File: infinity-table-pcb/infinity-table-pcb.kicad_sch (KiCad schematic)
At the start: 10 parts, among them J1 PJ-063AH, J2 Conn_01x05_Male, J3 Conn_01x10_Male

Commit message: forgot to save work
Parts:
- removed C1: 100nF, Capacitor_SMD:C_0805_2012Metric, symbol Device:C
- removed IO2, IO3, IO5, IO6: SolderJumper_3_Open, Jumper:SolderJumper-3_P1.3mm_Open_Pad1.0x1.5mm, symbol Jumper:SolderJumper_3_Open
- removed J2: Conn_01x05_Male, Connector_PinHeader_2.54mm:PinHeader_1x05_P2.54mm_Vertical, symbol Connector:Conn_01x05_Male
- removed J3: Conn_01x10_Male, Connector_PinHeader_2.54mm:PinHeader_1x10_P2.54mm_Vertical, symbol Connector:Conn_01x10_Male
- added RV?: R_Potentiometer, symbol Device:R_Potentiometer
- added U?: 74LVC8T245, symbol 74LVC8T245:74LVC8T245
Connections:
- net GND: now also RV?.1, U?.11 (GND), U?.12 (GND), U?.13 (GND)
- net at A1.19 (A0): now also RV?.2
- net +5V: now reaches A1.27 (+5V), C2.1
- net +5V: now also J1.1, RV?.3
- net D0: no longer names the net of A1.2 (D0/RX)
- net D1: no longer names the net of A1.1 (D1/TX)
- net D10: no longer names the net of A1.13 (D10)
- net D2: no longer names the net of A1.5 (D2)
- net D3: no longer names the net of A1.6 (D3)
- net D5: no longer names the net of A1.8 (D5)
- net D6: no longer names the net of A1.9 (D6)
- net D9: no longer names the net of A1.12 (D9)
- no-connect marks 15 -> 18
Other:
- moved on the sheet: C2, J1

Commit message: wip infinity-table-pcb
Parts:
- removed U?: 74LVC8T245, symbol 74LVC8T245:74LVC8T245
- added C? (x2): 1nF, Capacitor_SMD:C_0805_2012Metric, symbol Device:C
- added C? (x2): 0,1nF, Capacitor_SMD:C_0805_2012Metric, symbol Device:C
- added J?: Conn_01x04_Male, symbol Connector:Conn_01x04_Male
- added J?: Conn_01x10_Male, symbol Connector:Conn_01x10_Male
- added SW? (x2): SW_Push_Dual, symbol Switch:SW_Push_Dual
- added U?: TXS0108EPW, Package_SO:TSSOP-20_4.4x6.5mm_P0.65mm, symbol Logic_LevelTranslator:TXS0108EPW
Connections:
- net +5V: now also C?.2, J?.2 (Pin_2), U?.2 (VCCA)
- net GND: now also C?.1, C?.1, C?.2, C?.2, J?.1 (Pin_1), J?.1 (Pin_1), SW?.2, SW?.2, SW?.4, SW?.4, U?.10 (OE), U?.11 (GND); no longer A1.29 (GND)
- net at A1.10 (D7): now also U?.3 (A2)
- net at A1.11 (D8): now also U?.4 (A3)
- net at A1.12 (D9): now also U?.5 (A4)
- net at A1.13 (D10): now also U?.6 (A5)
- net at A1.14 (D11): now also U?.7 (A6)
- net at A1.15 (D12): now also U?.8 (A7)
- net at A1.16 (D13): now also U?.9 (A8)
- net at A1.6 (D3): now also J?.3 (Pin_3)
- net SW1: now reaches A1.7 (D4)
- net SW1: now also C?.2, SW?.1, SW?.3
- net SW2: now reaches A1.8 (D5)
- net SW2: now also C?.1, SW?.1, SW?.3
- net at A1.9 (D6): now also U?.1 (A1)
- new net: J?.2 (Pin_2), U?.12 (B8)
- new net: J?.3 (Pin_3), U?.13 (B7)
- new net: J?.4 (Pin_4), U?.14 (B6)
- new net: J?.5 (Pin_5), U?.15 (B5)
- new net: J?.6 (Pin_6), U?.16 (B4)
- new net: J?.7 (Pin_7), U?.17 (B3)
- new net: J?.8 (Pin_8), U?.18 (B2)
- new net: C?.1, J?.10 (Pin_10), U?.19 (VCCB)
- new net: J?.9 (Pin_9), U?.20 (B1)
- no-connect marks 18 -> 15
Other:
- note added: "LED connector"
- note added: "Level shifter"
- moved on the sheet: A1, C2, J1, RV?

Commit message: pcb first version done, but need to rework a bit
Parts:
- removed C2: 100nF, Capacitor_SMD:C_0805_2012Metric, symbol Device:C
- added R1: R, Resistor_SMD:R_0805_2012Metric, symbol Device:R
- C1, C3: renamed from C?; value 0,1nF -> 0,1uF
- J1: footprint SS_connectors:CUI_PJ-063AH-1 -> kicad-ss-libs:CUI_PJ-063AH
- J2: renamed from J?; footprint (none) -> Connector_PinHeader_2.54mm:PinHeader_1x04_P2.54mm_Vertical
- J3: renamed from J?; footprint (none) -> Connector_PinHeader_2.54mm:PinHeader_1x10_P2.54mm_Vertical
- RV1: renamed from RV?; footprint (none) -> Connector_PinHeader_2.54mm:PinHeader_1x03_P2.54mm_Vertical
- SW1, SW2: renamed from SW?; footprint (none) -> kicad-ss-libs:Push Button 12x12mm
- gave numbers to parts that had none: 3
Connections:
- net +5V: now also U1.19 (VCCB); no longer U1.2 (VCCA)
- net GND: now also A1.29 (GND), R1.2; no longer U1.10 (OE)
- net SW1: now also A1.8 (D5); no longer A1.7 (D4), SW1.3
- net SW2: now also A1.7 (D4); no longer A1.8 (D5), SW2.1
- net at A1.10 (D7): now also U1.18 (B2); no longer U1.3 (A2)
- net at A1.11 (D8): now also U1.17 (B3); no longer U1.4 (A3)
- net at A1.12 (D9): now also U1.16 (B4); no longer U1.5 (A4)
- net at A1.13 (D10): now also U1.15 (B5); no longer U1.6 (A5)
- net at A1.14 (D11): now also U1.14 (B6); no longer U1.7 (A6)
- net at A1.15 (D12): now also U1.13 (B7); no longer U1.8 (A7)
- net at A1.16 (D13): now also U1.12 (B8); no longer U1.9 (A8)
- net at A1.9 (D6): now also U1.20 (B1); no longer U1.1 (A1)
- net at J3.2 (Pin_2): now also U1.9 (A8); no longer U1.12 (B8)
- net at J3.3 (Pin_3): now also U1.8 (A7); no longer U1.13 (B7)
- net at J3.4 (Pin_4): now also U1.7 (A6); no longer U1.14 (B6)
- net at J3.5 (Pin_5): now also U1.6 (A5); no longer U1.15 (B5)
- net at J3.6 (Pin_6): now also U1.5 (A4); no longer U1.16 (B4)
- net at J3.7 (Pin_7): now also U1.4 (A3); no longer U1.17 (B3)
- net at J3.8 (Pin_8): now also U1.3 (A2); no longer U1.18 (B2)
- net at C3.1, J3.10 (Pin_10): now also U1.10 (OE), U1.2 (VCCA), R1.1; no longer U1.19 (VCCB)
- net at J3.9 (Pin_9): now also U1.1 (A1); no longer U1.20 (B1)
- no-connect marks 15 -> 18
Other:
- moved on the sheet: C1, J3

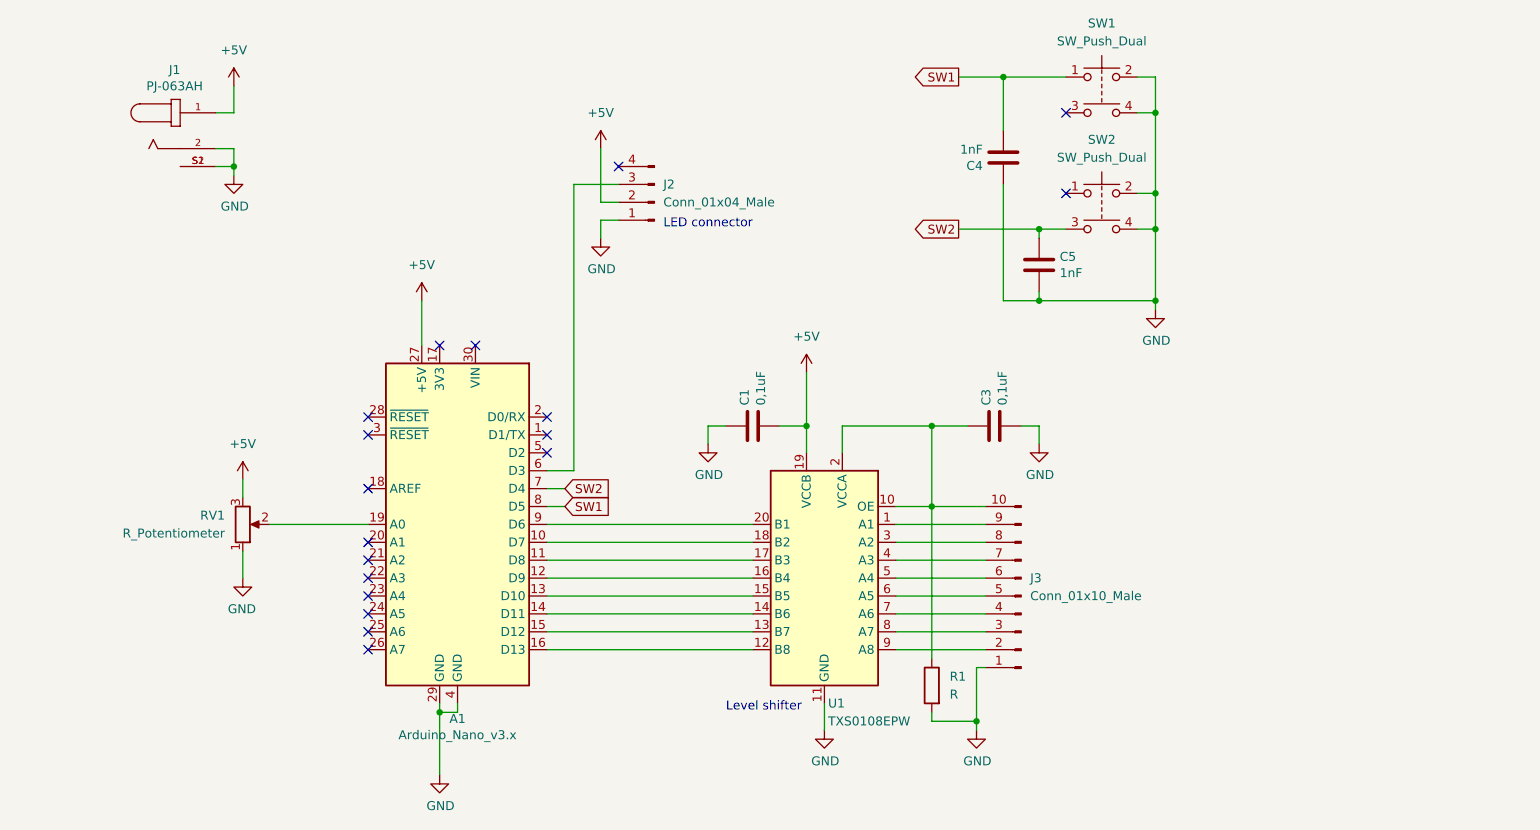
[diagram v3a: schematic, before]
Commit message: pcb ver 2 done. Maybe potentiometer footprint needs to be checked
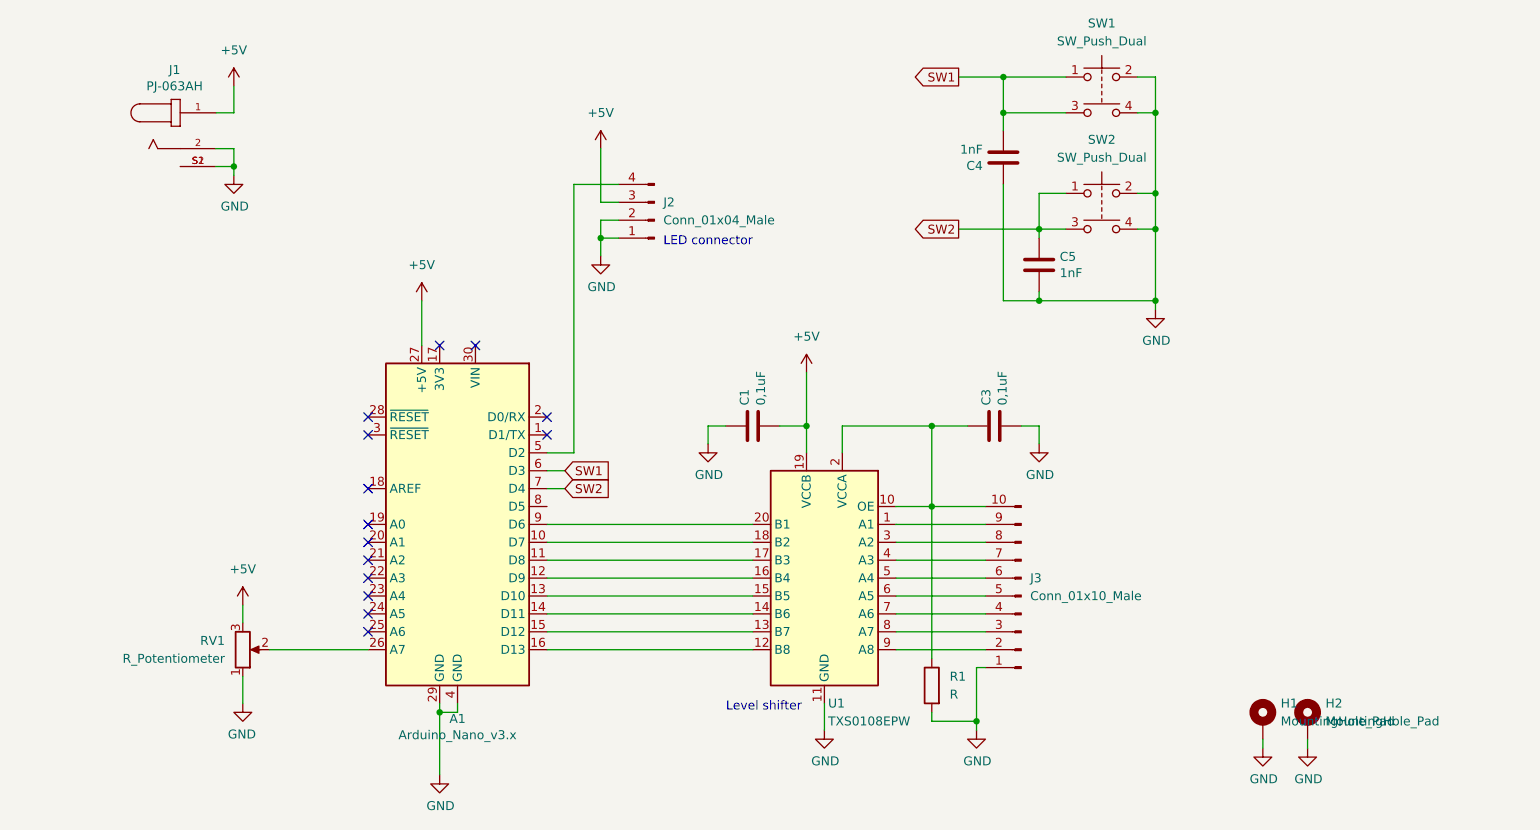
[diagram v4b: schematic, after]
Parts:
- added H1, H2: MountingHole_Pad, MountingHole:MountingHole_4.3mm_M4_Pad, symbol Mechanical:MountingHole_Pad
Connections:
- net +5V: now also J2.3 (Pin_3); no longer J2.2 (Pin_2)
- net GND: now also J2.2 (Pin_2), H1.1, H2.1
- net SW1: now also A1.6 (D3), SW1.3; no longer A1.8 (D5)
- net SW2: now also SW2.1
- net at A1.19 (A0): no longer RV1.2
- net at A1.26 (A7): now also RV1.2
- net at A1.5 (D2): now also J2.4 (Pin_4)
- no-connect marks 18 -> 14
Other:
- moved on the sheet: J2, RV1

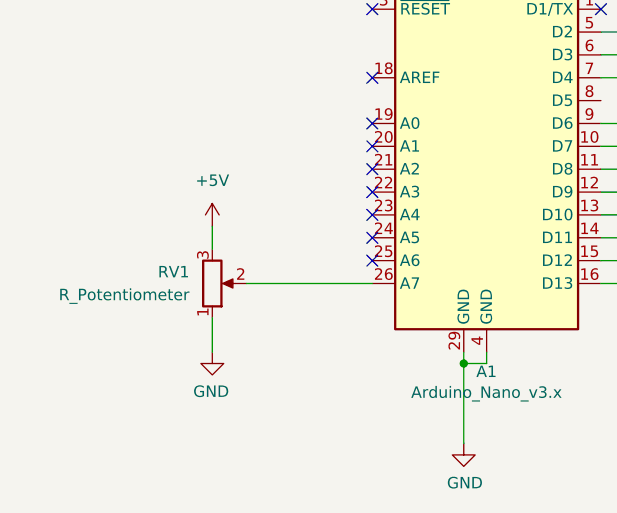
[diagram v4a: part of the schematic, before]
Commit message: Flip pcb design
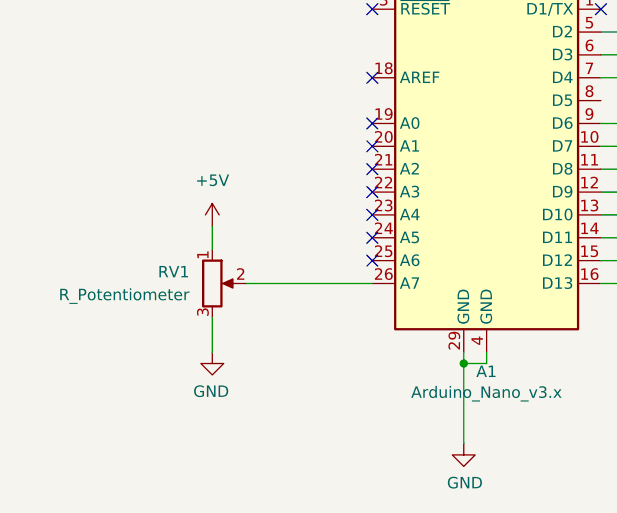
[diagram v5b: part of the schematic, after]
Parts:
- RV1: footprint Connector_PinHeader_2.54mm:PinHeader_1x03_P2.54mm_Vertical -> kicad-ss-libs:Potentiometer Thruhole
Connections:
- net +5V: now also RV1.1; no longer RV1.3
- net GND: now also RV1.3; no longer RV1.1
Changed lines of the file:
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@@
     (pin "4")
   )
-  (symbol (lib_id "Device:R_Potentiometer") (at 96.52 130.81 0) (mirror x) (unit 1)
+  (symbol (lib_id "Device:R_Potentiometer") (at 96.52 130.81 0) (unit 1)
     (in_bom yes) (on_board yes) (fields_autoplaced)
     (property "Reference" "RV1" (id 0) (at 93.98 129.5399 0)
@@
       (effects (font (size 1.27 1.27)) (justify right))
     )
-    (property "Footprint" "Connector_PinHeader_2.54mm:PinHeader_1x03_P2.54mm_Vertical" (id 2) (at 96.52 130.81 0)
+    (property "Footprint" "kicad-ss-libs:Potentiometer Thruhole" (id 2) (at 96.52 130.81 0)
       (effects (font (size 1.27 1.27)) hide)
     )
@@
     )
     (path "/83abc281-50cb-48bb-8e44-6469265be44c"
-      (reference "RV1") (unit 1) (value "R_Potentiometer") (footprint "Connector_PinHeader_2.54mm:PinHeader_1x03_P2.54mm_Vertical")
+      (reference "RV1") (unit 1) (value "R_Potentiometer") (footprint "kicad-ss-libs:Potentiometer Thruhole")
     )
     (path "/830a7ed6-ee6e-4930-b0e3-7063f8168620"

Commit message: power supply on the right, led connector on the left. idk
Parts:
- RV1: footprint kicad-ss-libs:Potentiometer Thruhole -> kicad-ss-libs:Potentiometer Pads
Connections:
- net +5V: now also J2.4 (Pin_4); no longer J2.3 (Pin_3)
- net SW1: no longer SW1.1
- net SW2: no longer SW2.1
- net at A1.5 (D2): now also J2.3 (Pin_3); no longer J2.4 (Pin_4)
- no-connect marks 14 -> 16
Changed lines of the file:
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@@
   (junction (at 226.06 81.28) (diameter 0) (color 0 0 0 0)
   )
+  (junction (at 204.47 54.61) (diameter 0) (color 0 0 0 0)
+  )
   (junction (at 226.06 71.12) (diameter 0) (color 0 0 0 0)
   )
   (junction (at 200.66 140.97) (diameter 0) (color 0 0 0 0)
   )
-  (junction (at 204.47 49.53) (diameter 0) (color 0 0 0 0)
-  )
   (junction (at 176.53 99.06) (diameter 0) (color 0 0 0 0)
   )
@@
   )
   (junction (at 194.31 110.49) (diameter 0) (color 0 0 0 0)
-  )
-  (junction (at 204.47 54.61) (diameter 0) (color 0 0 0 0)
   )
   (junction (at 226.06 66.04) (diameter 0) (color 0 0 0 0)
@@
   (no_connect (at 114.3 128.27))
   (no_connect (at 114.3 115.57))
+  (no_connect (at 213.36 66.04))
   (no_connect (at 139.7 97.79))
+  (no_connect (at 213.36 49.53))
   (no_connect (at 139.7 100.33))
   (no_connect (at 114.3 118.11))
@@
     (stroke (width 0) (type default) (color 0 0 0 0))
   )
-  (wire (pts (xy 204.47 49.53) (xy 213.36 49.53))
-    (stroke (width 0) (type default) (color 0 0 0 0))
-  )
   (wire (pts (xy 162.56 99.06) (xy 162.56 101.6))
     (stroke (width 0) (type default) (color 0 0 0 0))
@@
     (stroke (width 0) (type default) (color 0 0 0 0))
   )
-  (wire (pts (xy 149.86 64.77) (xy 143.51 64.77))
-    (stroke (width 0) (type default) (color 0 0 0 0))
-  )
   (wire (pts (xy 209.55 81.28) (xy 226.06 81.28))
     (stroke (width 0) (type default) (color 0 0 0 0))
@@
     (stroke (width 0) (type default) (color 0 0 0 0))
   )
+  (wire (pts (xy 149.86 64.77) (xy 147.32 64.77))
+    (stroke (width 0) (type default) (color 0 0 0 0))
+  )
   (wire (pts (xy 198.12 71.12) (xy 209.55 71.12))
     (stroke (width 0) (type default) (color 0 0 0 0))
@@
     (stroke (width 0) (type default) (color 0 0 0 0))
   )
-  (wire (pts (xy 198.12 49.53) (xy 204.47 49.53))
+  (wire (pts (xy 198.12 54.61) (xy 204.47 54.61))
     (stroke (width 0) (type default) (color 0 0 0 0))
   )
@@
     (stroke (width 0) (type default) (color 0 0 0 0))
   )
-  (wire (pts (xy 147.32 59.69) (xy 147.32 67.31))
-    (stroke (width 0) (type default) (color 0 0 0 0))
-  )
   (wire (pts (xy 139.7 113.03) (xy 168.91 113.03))
     (stroke (width 0) (type default) (color 0 0 0 0))
@@
     (stroke (width 0) (type default) (color 0 0 0 0))
   )
-  (wire (pts (xy 147.32 67.31) (xy 149.86 67.31))
-    (stroke (width 0) (type default) (color 0 0 0 0))
-  )
   (wire (pts (xy 179.07 138.43) (xy 179.07 142.24))
     (stroke (width 0) (type default) (color 0 0 0 0))
@@
     (stroke (width 0) (type default) (color 0 0 0 0))
   )
-  (wire (pts (xy 213.36 66.04) (xy 209.55 66.04))
-    (stroke (width 0) (type default) (color 0 0 0 0))
-  )
   (wire (pts (xy 92.71 62.23) (xy 95.25 62.23))
     (stroke (width 0) (type default) (color 0 0 0 0))
@@
     (stroke (width 0) (type default) (color 0 0 0 0))
   )
-  (wire (pts (xy 204.47 49.53) (xy 204.47 54.61))
+  (wire (pts (xy 143.51 67.31) (xy 149.86 67.31))
     (stroke (width 0) (type default) (color 0 0 0 0))
   )
@@
     (stroke (width 0) (type default) (color 0 0 0 0))
   )
+  (wire (pts (xy 147.32 64.77) (xy 147.32 59.69))
+    (stroke (width 0) (type default) (color 0 0 0 0))
+  )
   (wire (pts (xy 139.7 128.27) (xy 168.91 128.27))
     (stroke (width 0) (type default) (color 0 0 0 0))
@@
     (stroke (width 0) (type default) (color 0 0 0 0))
   )
-  (wire (pts (xy 209.55 66.04) (xy 209.55 71.12))
-    (stroke (width 0) (type default) (color 0 0 0 0))
-  )
   (wire (pts (xy 241.3 143.51) (xy 241.3 144.78))
     (stroke (width 0) (type default) (color 0 0 0 0))
@@
     (stroke (width 0) (type default) (color 0 0 0 0))
   )
-  (wire (pts (xy 143.51 64.77) (xy 143.51 102.87))
-    (stroke (width 0) (type default) (color 0 0 0 0))
-  )
   (wire (pts (xy 139.7 125.73) (xy 168.91 125.73))
     (stroke (width 0) (type default) (color 0 0 0 0))
@@
   )
   (wire (pts (xy 194.31 140.97) (xy 194.31 139.7))
+    (stroke (width 0) (type default) (color 0 0 0 0))
+  )
+  (wire (pts (xy 143.51 67.31) (xy 143.51 102.87))
     (stroke (width 0) (type default) (color 0 0 0 0))
   )
@@
     )
   )
-  (global_label "SW1" (shape output) (at 198.12 49.53 180) (fields_autoplaced)
+  (global_label "SW1" (shape output) (at 198.12 54.61 180) (fields_autoplaced)
     (effects (font (size 1.27 1.27)) (justify right))
-    (property "Intersheet References" "${INTERSHEET_REFS}" (id 0) (at 191.9253 49.6094 0)
+    (property "Intersheet References" "${INTERSHEET_REFS}" (id 0) (at 191.9253 54.6894 0)
       (effects (font (size 1.27 1.27)) (justify right) hide)
     )
@@
       (effects (font (size 1.27 1.27)) (justify right))
     )
-    (property "Footprint" "kicad-ss-libs:Potentiometer Thruhole" (id 2) (at 96.52 130.81 0)
+    (property "Footprint" "kicad-ss-libs:Potentiometer Pads" (id 2) (at 96.52 130.81 0)
       (effects (font (size 1.27 1.27)) hide)
     )
@@
     )
     (path "/83abc281-50cb-48bb-8e44-6469265be44c"
-      (reference "RV1") (unit 1) (value "R_Potentiometer") (footprint "kicad-ss-libs:Potentiometer Thruhole")
+      (reference "RV1") (unit 1) (value "R_Potentiometer") (footprint "kicad-ss-libs:Potentiometer Pads")
     )
     (path "/830a7ed6-ee6e-4930-b0e3-7063f8168620"

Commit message: moar holes
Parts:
- added H3, H4: MountingHole, MountingHole:MountingHole_2.2mm_M2, symbol Mechanical:MountingHole
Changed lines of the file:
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@@
     (pin "1")
+  )
+  (symbol (lib_id "Mechanical:MountingHole") (at 260.35 139.7 0) (unit 1)
+    (in_bom yes) (on_board yes) (fields_autoplaced)
+    (property "Reference" "H4" (id 0) (at 262.89 138.4299 0)
+      (effects (font (size 1.27 1.27)) (justify left))
+    )
+    (property "Value" "MountingHole" (id 1) (at 262.89 140.9699 0)
+      (effects (font (size 1.27 1.27)) (justify left))
+    )
+    (property "Footprint" "MountingHole:MountingHole_2.2mm_M2" (id 2) (at 260.35 139.7 0)
+      (effects (font (size 1.27 1.27)) hide)
+    )
+    (property "Datasheet" "~" (id 3) (at 260.35 139.7 0)
+      (effects (font (size 1.27 1.27)) hide)
+    )
   )
   (symbol (lib_id "Mechanical:MountingHole_Pad") (at 247.65 140.97 0) (unit 1)
@@
     )
     (pin "1")
+  )
+  (symbol (lib_id "Mechanical:MountingHole") (at 254 139.7 0) (unit 1)
+    (in_bom yes) (on_board yes) (fields_autoplaced)
+    (property "Reference" "H3" (id 0) (at 256.54 138.4299 0)
+      (effects (font (size 1.27 1.27)) (justify left))
+    )
+    (property "Value" "MountingHole" (id 1) (at 256.54 140.9699 0)
+      (effects (font (size 1.27 1.27)) (justify left))
+    )
+    (property "Footprint" "MountingHole:MountingHole_2.2mm_M2" (id 2) (at 254 139.7 0)
+      (effects (font (size 1.27 1.27)) hide)
+    )
+    (property "Datasheet" "~" (id 3) (at 254 139.7 0)
+      (effects (font (size 1.27 1.27)) hide)
+    )
   )
   (symbol (lib_id "power:GND") (at 247.65 144.78 0) (unit 1)
@@
       (reference "H2") (unit 1) (value "MountingHole_Pad") (footprint "MountingHole:MountingHole_4.3mm_M4_Pad")
     )
+    (path "/65fd9534-1b91-42a6-8ecd-7a42d8ae4ade"
+      (reference "H3") (unit 1) (value "MountingHole") (footprint "MountingHole:MountingHole_2.2mm_M2")
+    )
+    (path "/28d92791-e03b-49b7-ab76-0b79e48b37f2"
+      (reference "H4") (unit 1) (value "MountingHole") (footprint "MountingHole:MountingHole_2.2mm_M2")
+    )
     (path "/00000000-0000-0000-0000-00005bf7fa3a"
